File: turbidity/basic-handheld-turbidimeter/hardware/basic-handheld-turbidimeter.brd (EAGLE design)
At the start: 45.1 x 63.5 mm, 37 parts, among them Q1 16.000, U1 ATMEGA328P-PU

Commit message: added OSHW logo to main board, added seven segment helper board
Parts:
- added U$5: (no value), SparkFun-Aesthetics:OSHW-LOGO-M
- 2.4V_ZENER: value DIODE-ZENERPTH -> DNP
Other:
- board text added: "AWQUA Basic Handheld Turbidimeter 2014/12/01"
- board text removed: "AWQUA Initiative Basic Handheld Turbidimeter Blue Turtle 2014/12/01"
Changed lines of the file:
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@@
 <?xml version="1.0" encoding="utf-8"?>
 <!DOCTYPE eagle SYSTEM "eagle.dtd">
-<eagle version="7.2.0">
+<eagle version="7.3.0">
 <drawing>
 <settings>
@@
 <text x="31.115" y="60.325" size="1.778" layer="25" rot="MR0">-</text>
 <text x="8.89" y="60.325" size="1.778" layer="25" rot="MR0">-</text>
-<text x="35.56" y="43.18" size="1.778" layer="25" rot="MR0">*</text>
+<text x="35.56" y="45.085" size="1.778" layer="25" rot="MR270">*</text>
 <text x="27.94" y="14.605" size="1.778" layer="25" rot="MR0">*</text>
 <text x="31.115" y="54.61" size="1.778" layer="25" rot="MR0">-</text>
 <text x="13.335" y="54.61" size="1.778" layer="25" rot="MR0">-</text>
 <text x="34.29" y="29.845" size="1.6764" layer="26" rot="MR270" align="center"></text>
-<text x="20.955" y="37.465" size="1.778" layer="26" rot="MR270" align="center">AWQUA Initiative
-Basic Handheld Turbidimeter
-Blue Turtle
+<text x="34.925" y="31.75" size="1.778" layer="26" rot="MR270" align="center">AWQUA
+Basic Handheld
+Turbidimeter
 2014/12/01
 </text>
@@
 <attribute name="SUPPLIER" value="Atmel" x="57.785" y="12.7" size="1.778" layer="27" display="off"/>
 <attribute name="OC_FARNELL" value="1715487" x="57.785" y="12.7" size="1.778" layer="27" display="off"/>
-<attribute name="VALUE" x="20.32" y="47.2694" size="2.0828" layer="25" ratio="10" rot="SR270"/>
+<attribute name="VALUE" x="20.955" y="46.6344" size="2.0828" layer="25" ratio="10" rot="SR270"/>
 </element>
 <element name="4XAA" library="pinhead" package="1X02" value="" x="11.43" y="59.69" smashed="yes">
@@
 </element>
 <element name="SENSOR" library="pinhead" package="1X03" value="" x="39.37" y="49.53" smashed="yes" rot="R180">
-<attribute name="NAME" x="43.2562" y="52.7812" size="1.27" layer="25" ratio="10" rot="R180"/>
+<attribute name="NAME" x="35.6362" y="45.0088" size="1.27" layer="25" ratio="10" rot="R90"/>
 <attribute name="VALUE" x="43.18" y="52.705" size="1.27" layer="27" rot="R180"/>
 </element>
@@
 <attribute name="VALUE" x="35.56" y="42.545" size="1.27" layer="27"/>
 </element>
-<element name="2.4V_ZENER" library="SparkFun-DiscreteSemi" package="DIODE-ZENER" value="DIODE-ZENERPTH" x="2.54" y="12.065" smashed="yes" rot="R270">
+<element name="2.4V_ZENER" library="SparkFun-DiscreteSemi" package="DIODE-ZENER" value="DNP" x="2.54" y="12.065" smashed="yes" rot="R270">
 <attribute name="NAME" x="3.81" y="15.875" size="0.9144" layer="25" rot="R270"/>
 </element>
@@
 <element name="U$4" library="holes" package="2,8" value="" x="41.275" y="3.81"/>
 <element name="C6" library="SparkFun-Capacitors" package="CAP-PTH-SMALLEZ" value="100nF" x="31.115" y="48.895" smashed="yes" rot="R270">
-<attribute name="VALUE" x="33.02" y="49.53" size="0.9144" layer="25" rot="R270"/>
-</element>
+<attribute name="VALUE" x="29.21" y="50.8" size="0.9144" layer="25"/>
+</element>
+<element name="U$5" library="SparkFun-Aesthetics" package="OSHW-LOGO-M" value="" x="41.91" y="53.34"/>
 </elements>
 <signals>

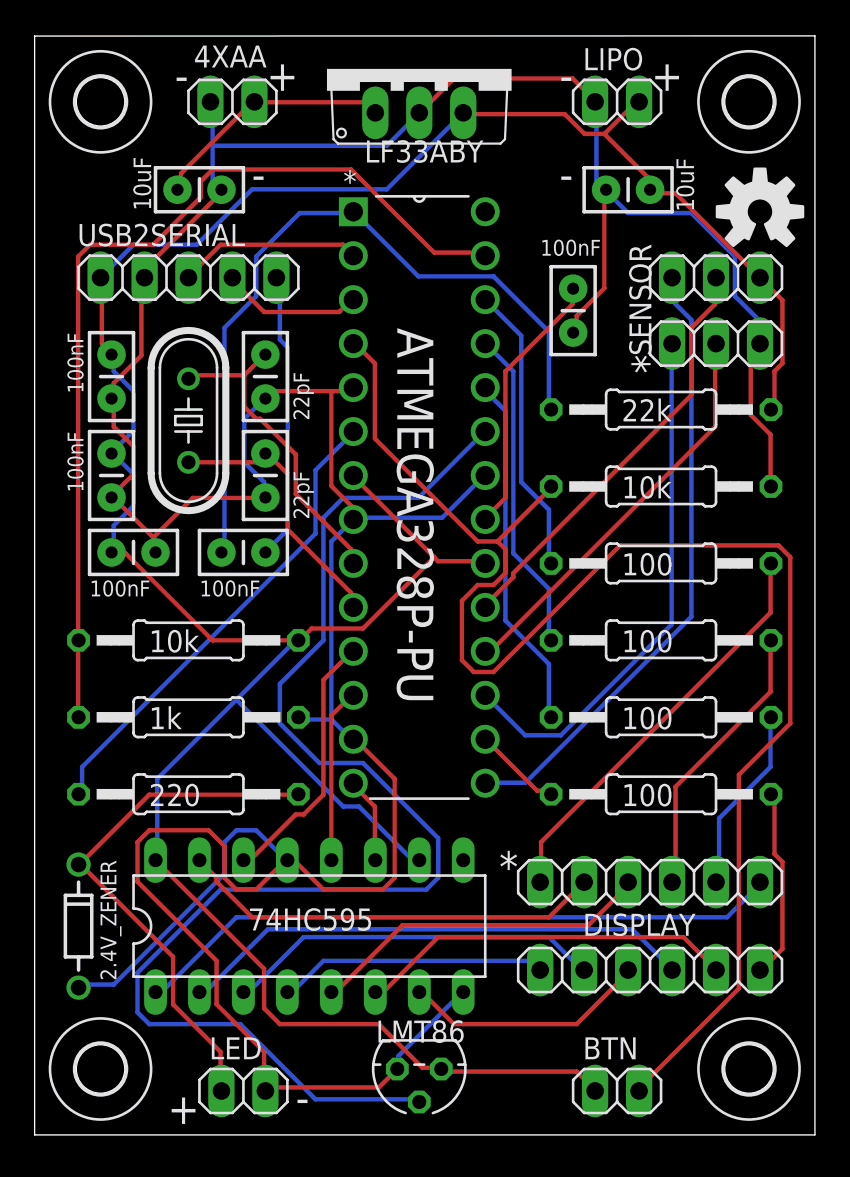
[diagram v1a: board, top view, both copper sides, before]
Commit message: added current regulator for IR LED
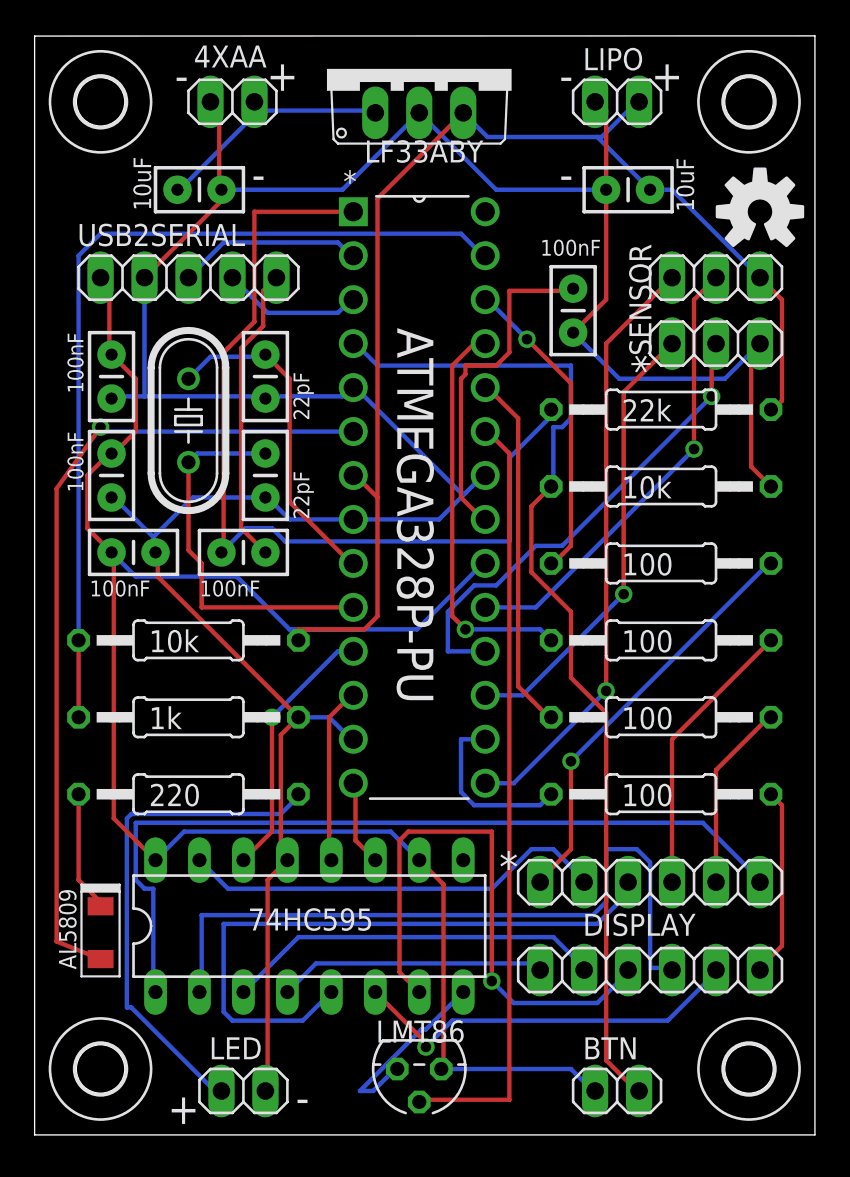
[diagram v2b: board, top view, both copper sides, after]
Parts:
- removed 2.4V_ZENER: DNP, SparkFun-DiscreteSemi:DIODE-ZENER
- added U$6: AL5809, awqua_eagle_library:AL5809
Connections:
- new net N$2: R10.2, U$6.OUT
- net GND: no longer 2.4V_ZENER.P$2
- net LED: no longer 2.4V_ZENER.P$1
- net PD4: now also U$6.IN; no longer R10.2
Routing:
- net GND: track 223.3 -> 180.8 mm
- net PC0: track 78.9 -> 44.5 mm
- net PD2: track 85.7 -> 58.9 mm
- net PD4: track 27.5 -> 48.0 mm, vias 0 -> 1
- net 595H: track 14.2 -> 32.7 mm, vias 0 -> 1
- net 595F: track 20.0 -> 36.9 mm
- net 595C: track 29.9 -> 41.6 mm
- net 595B: track 37.7 -> 48.1 mm
- net PC6: track 43.3 -> 52.4 mm
- net N$2: track 0.00 -> 7.00 mm
- net PB7: track 15.7 -> 22.1 mm
- net PB2: track 5.15 -> 10.2 mm
- net PB3: track 30.6 -> 26.1 mm, vias 0 -> 1
- net PB4: track 23.6 -> 28.0 mm, vias 0 -> 1
- net PC2: track 18.8 -> 23.2 mm, vias 0 -> 1
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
